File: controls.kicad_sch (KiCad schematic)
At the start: 71 parts, among them SW501 SW, SW502 SW, SW503 SW, SW504 SW, SW505 SW, SW506 SW, SW507 SW, SW508 SW, SW509 SW, SW510 SW, SW511 SW_Push, SW512 SW_Push, SW513 SW, SW514 SW, SW515 SW, SW516 SW, SW517 RotaryEncoder_Switch, SW518 SW, SW519 SW, SW520 RotaryEncoder_Switch, SW521 SW, SW522 SW, U501 74HC165, U502 74HC165

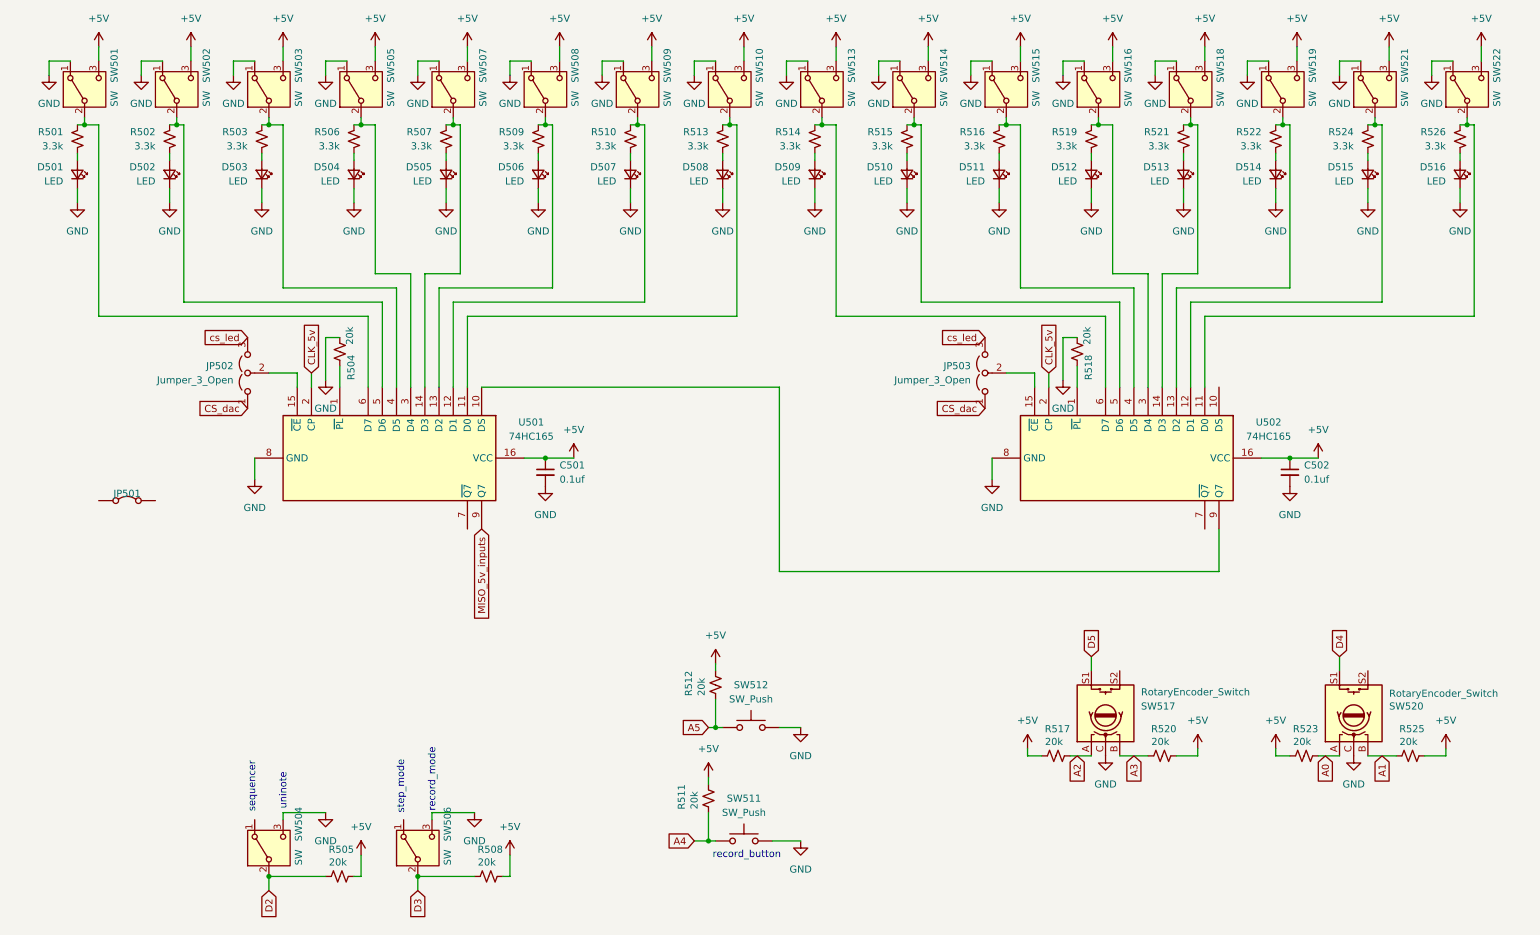
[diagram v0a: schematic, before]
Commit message: schematic done, routed dac ladder
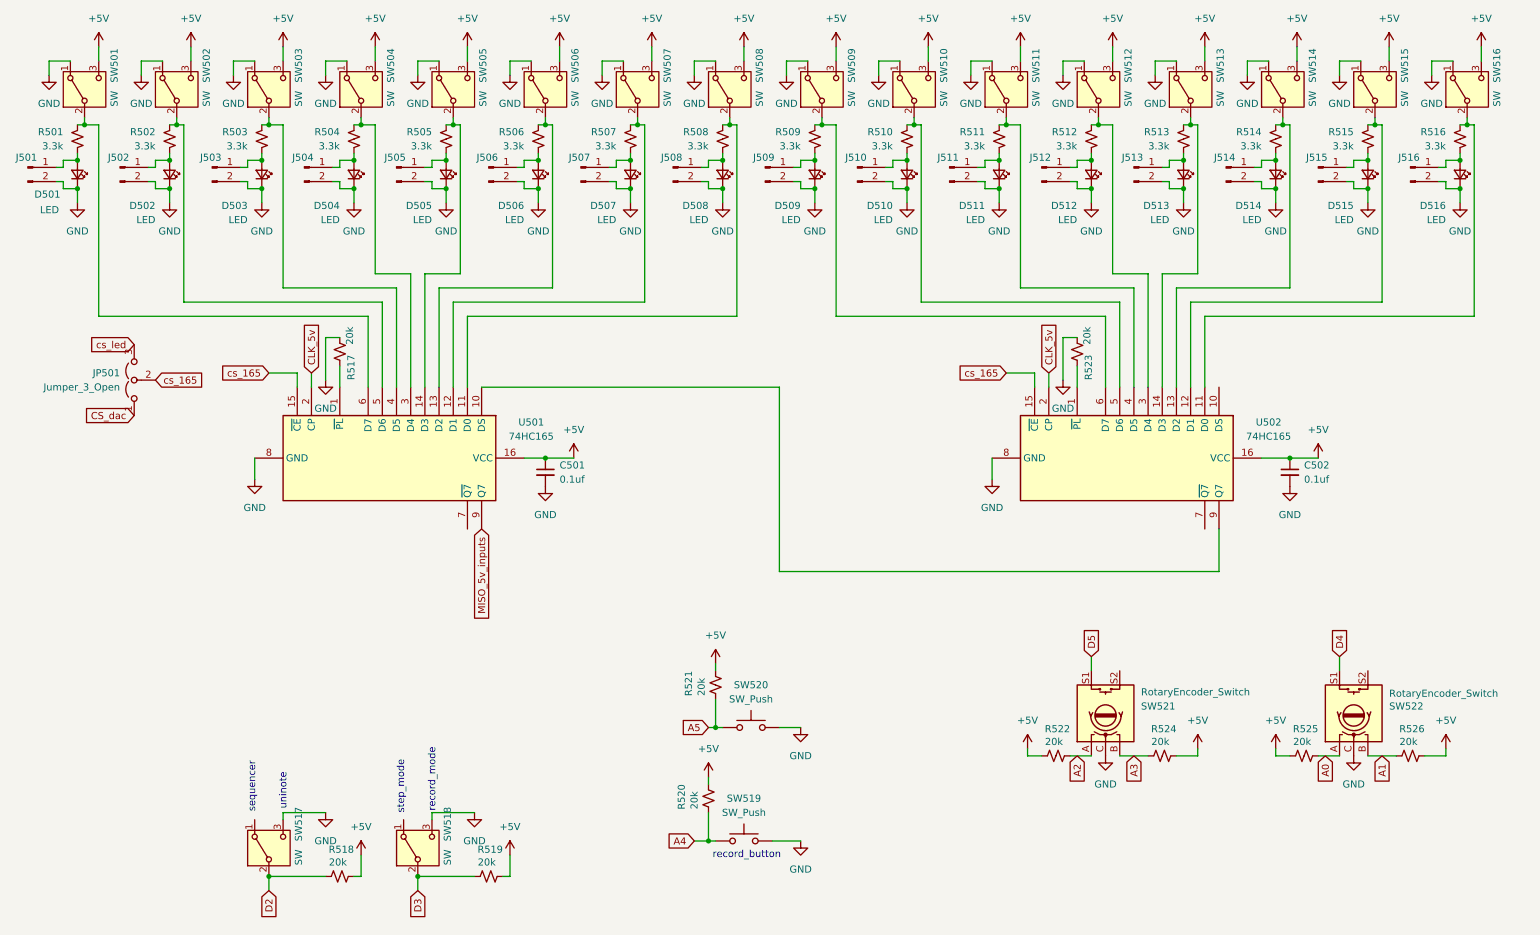
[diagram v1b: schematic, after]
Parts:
- removed JP501: ~, Jumper:SolderJumper-2_P1.3mm_Bridged_RoundedPad1.0x1.5mm, symbol Jumper:Jumper_2_Bridged
- removed JP503: Jumper_3_Open, Connector_PinHeader_2.54mm:PinHeader_1x03_P2.54mm_Vertical, symbol Jumper:Jumper_3_Open
- added J501, J502, J503, J504, J505, J506, J507, J508, J509, J510, J511, J512, J513, J514, J515, J516: Conn_01x02_Pin, Connector_PinSocket_2.54mm:PinSocket_1x02_P2.54mm_Vertical, symbol Connector:Conn_01x02_Pin
- renumbered JP502 to JP501, R506 to R504, R507 to R505, R509 to R506, R510 to R507, R513 to R508, R514 to R509, R515 to R510, R516 to R511, R519 to R512, R521 to R513, R522 to R514, R524 to R515, R526 to R516, R504 to R517, R505 to R518, R508 to R519, R511 to R520, R512 to R521, R517 to R522, R518 to R523, R520 to R524, R523 to R525, R525 to R526, SW505 to SW504, SW507 to SW505, SW508 to SW506, SW509 to SW507, SW510 to SW508, SW513 to SW509, SW514 to SW510, SW515 to SW511, SW516 to SW512, SW518 to SW513, SW519 to SW514, SW521 to SW515, SW522 to SW516, SW504 to SW517, SW506 to SW518, SW511 to SW519, SW512 to SW520, SW517 to SW521, SW520 to SW522
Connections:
- net GND: now also J501.2 (Pin_2), J502.2 (Pin_2), J503.2 (Pin_2), J504.2 (Pin_2), J505.2 (Pin_2), J506.2 (Pin_2), J507.2 (Pin_2), J508.2 (Pin_2), J509.2 (Pin_2), J510.2 (Pin_2), J511.2 (Pin_2), J512.2 (Pin_2), J513.2 (Pin_2), J514.2 (Pin_2), J515.2 (Pin_2), J516.2 (Pin_2)
- net at D503.2 (A), R503.2: now also J503.1 (Pin_1)
- net at D512.2 (A), R512.2: now also J512.1 (Pin_1)
- net cs_165: now reaches JP501.2 (C), U501.15 (~{CE})
- net cs_165: now also U502.15 (~{CE})
- net at D506.2 (A), R506.2: now also J506.1 (Pin_1)
- net at D515.2 (A), R515.2: now also J515.1 (Pin_1)
- net at D516.2 (A), R516.2: now also J516.1 (Pin_1)
- net at D508.2 (A), R508.2: now also J508.1 (Pin_1)
- net at D514.2 (A), R514.2: now also J514.1 (Pin_1)
- net at D507.2 (A), R507.2: now also J507.1 (Pin_1)
- net at D504.2 (A), R504.2: now also J504.1 (Pin_1)
- net at D511.2 (A), R511.2: now also J511.1 (Pin_1)
- net at D501.2 (A), R501.2: now also J501.1 (Pin_1)
- net at D509.2 (A), R509.2: now also J509.1 (Pin_1)
- net at D510.2 (A), R510.2: now also J510.1 (Pin_1)
- net at D505.2 (A), R505.2: now also J505.1 (Pin_1)
- net at D513.2 (A), R513.2: now also J513.1 (Pin_1)
- net at D502.2 (A), R502.2: now also J502.1 (Pin_1)
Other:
- moved on the sheet: JP501

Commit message: grouped components in board
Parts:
- SW521, SW522: footprint rotary:RotaryEncoder_Alps_EC11E_Vertical_H20mm -> RotaryEncoder:RotaryEncoder_Alps_EC11E-Switch_Vertical_H20mm
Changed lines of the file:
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@@
 			)
 		)
-		(property "Footprint" "rotary:RotaryEncoder_Alps_EC11E_Vertical_H20mm"
+		(property "Footprint" "RotaryEncoder:RotaryEncoder_Alps_EC11E-Switch_Vertical_H20mm"
 			(at 202.946 151.13 0)
 			(effects
@@
 			)
 		)
-		(property "Footprint" "rotary:RotaryEncoder_Alps_EC11E_Vertical_H20mm"
+		(property "Footprint" "RotaryEncoder:RotaryEncoder_Alps_EC11E-Switch_Vertical_H20mm"
 			(at 247.396 151.13 0)
 			(effects

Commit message: FINISHED ROUTING
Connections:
- net D4: now also SW521.S1; no longer SW522.S1
- net D5: now also SW522.S1; no longer SW521.S1
- net GND: now also SW521.S2, SW522.S2
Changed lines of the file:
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@@
 	(wire
 		(pts
+			(xy 214.63 135.89) (xy 209.55 135.89)
+		)
+		(stroke
+			(width 0)
+			(type default)
+		)
+	)
+	(wire
+		(pts
 			(xy 220.98 48.26) (xy 220.98 46.99)
 		)
@@
 	(wire
 		(pts
+			(xy 259.08 135.89) (xy 254 135.89)
+		)
+		(stroke
+			(width 0)
+			(type default)
+		)
+	)
+	(wire
+		(pts
 			(xy 266.7 49.53) (xy 267.97 49.53)
 		)
@@
 	(wire
 		(pts
+			(xy 254 135.89) (xy 254 139.7)
+		)
+		(stroke
+			(width 0)
+			(type default)
+		)
+	)
+	(wire
+		(pts
 			(xy 34.29 33.02) (xy 34.29 30.48)
 		)
@@
 	(wire
 		(pts
+			(xy 209.55 135.89) (xy 209.55 139.7)
+		)
+		(stroke
+			(width 0)
+			(type default)
+		)
+	)
+	(wire
+		(pts
 			(xy 171.45 41.91) (xy 172.72 41.91)
 		)
@@
 	(global_label "D5"
 		(shape input)
-		(at 204.47 137.16 90)
+		(at 248.92 137.16 90)
 		(fields_autoplaced yes)
 		(effects
@@
 		)
 		(property "Intersheetrefs" "${INTERSHEET_REFS}"
-			(at 204.47 131.6953 90)
+			(at 248.92 131.6953 90)
 			(effects
 				(font
@@
 	(global_label "D4"
 		(shape input)
-		(at 248.92 137.16 90)
+		(at 204.47 137.16 90)
 		(fields_autoplaced yes)
 		(effects
@@
 		)
 		(property "Intersheetrefs" "${INTERSHEET_REFS}"
-			(at 248.92 131.6953 90)
+			(at 204.47 131.6953 90)
 			(effects
 				(font
@@
 	)
 	(symbol
+		(lib_id "power:GND")
+		(at 259.08 135.89 0)
+		(mirror y)
+		(unit 1)
+		(exclude_from_sim no)
+		(in_bom yes)
+		(on_board yes)
+		(dnp no)
+		(fields_autoplaced yes)
+		(property "Reference" "#PWR0572"
+			(at 259.08 142.24 0)
+			(effects
+				(font
+					(size 1.27 1.27)
+				)
+				(hide yes)
+			)
+		)
+		(property "Value" "GND"
+			(at 259.08 140.97 0)
+			(effects
+				(font
+					(size 1.27 1.27)
+				)
+			)
+		)
+		(property "Footprint" ""
+			(at 259.08 135.89 0)
+			(effects
+				(font
+					(size 1.27 1.27)
+				)
+				(hide yes)
+			)
+		)
+		(property "Datasheet" ""
+			(at 259.08 135.89 0)
+			(effects
+				(font
+					(size 1.27 1.27)
+				)
+				(hide yes)
+			)
+		)
+		(property "Description" "Power symbol creates a global label with name \"GND\" , ground"
+			(at 259.08 135.89 0)
+			(effects
+				(font
+					(size 1.27 1.27)
+				)
+				(hide yes)
+			)
+		)
+		(pin "1"
+		)
+		(instances
+			(project "nano_sequencer"
+				(path "/335d65e6-88b4-479c-8bfd-74e13066bd23/9e5f6a1e-2800-4dbb-afe9-cca317b92691"
+					(reference "#PWR0572")
+					(unit 1)
+				)
+			)
+		)
+	)
+	(symbol
 		(lib_id "Switch:SW_SPDT")
 		(at 238.76 35.56 90)
@@
 					(unit 1)
 				)
+			)
+		)
+	)
+	(symbol
+		(lib_id "power:GND")
+		(at 214.63 135.89 0)
+		(mirror y)
+		(unit 1)
+		(exclude_from_sim no)
+		(in_bom yes)
+		(on_board yes)
+		(dnp no)
+		(fields_autoplaced yes)
+		(property "Reference" "#PWR0571"
+			(at 214.63 142.24 0)
+			(effects
+				(font
+					(size 1.27 1.27)
+				)
+				(hide yes)
+			)
+		)
+		(property "Value" "GND"
+			(at 214.63 140.97 0)
+			(effects
+				(font
+					(size 1.27 1.27)
+				)
+			)
+		)
+		(property "Footprint" ""
+			(at 214.63 135.89 0)
+			(effects
+				(font
+					(size 1.27 1.27)
+				)
+				(hide yes)
+			)
+		)
+		(property "Datasheet" ""
+			(at 214.63 135.89 0)
+			(effects
+				(font
+					(size 1.27 1.27)
+				)
+				(hide yes)
+			)
+		)
+		(property "Description" "Power symbol creates a global label with name \"GND\" , ground"
+			(at 214.63 135.89 0)
+			(effects
+				(font
+					(size 1.27 1.27)
+				)
+				(hide yes)
+			)
+		)
+		(pin "1"
+		)
+		(instances
+			(project "nano_sequencer"
+				(path "/335d65e6-88b4-479c-8bfd-74e13066bd23/9e5f6a1e-2800-4dbb-afe9-cca317b92691"
+					(reference "#PWR0571")
+					(unit 1)
+				)

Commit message: added lcsc part numbers and fabrication files
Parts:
- C501, C502: footprint LED_SMD:LED_0805_2012Metric_Pad1.15x1.40mm_HandSolder -> Capacitor_SMD:C_0805_2012Metric_Pad1.18x1.45mm_HandSolder; LCSC PN (none) -> C49678
- D501, D502, D503, D504, D505, D506, D507, D508, D509, D510, D511, D512, D513, D514, D515, D516: LCSC PN (none) -> C2297
- R501, R502, R503, R504, R505, R506, R507, R508, R509, R510, R511, R512, R513, R514, R515, R516: value 3.3k -> 2k; LCSC PN (none) -> C17604
- R517, R518, R519, R520, R521, R522, R523, R524, R525, R526: LCSC PN (none) -> C4328
- U501, U502: LCSC PN (none) -> C5613
